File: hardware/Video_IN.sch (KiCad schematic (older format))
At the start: 15 parts, among them U4 DS90CF363AMTD

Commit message: Renaming wires
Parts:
- U4: value DS90CF363AMTD -> DS90CF36B
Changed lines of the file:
@@
 P 7300 3000
 F 0 "U4" H 7300 4770 50  0000 C CNN
-F 1 "DS90CF363AMTD" H 7300 4679 50  0000 C CNN
+F 1 "DS90CF36B" H 7300 4679 50  0000 C CNN
 F 2 "DS90CF364AMTD:SOP50P800X110-48N" H 7300 3000 50  0001 L BNN
 F 3 "41K1941" H 7300 3000 50  0001 L BNN

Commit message: Routing board
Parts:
- R16: renamed from R?; footprint (none) -> Resistor_SMD:R_0805_2012Metric
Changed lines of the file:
@@
 	3550 1850 3650 1850
 $Comp
-L antena:R R?
+L antena:R R16
 U 1 1 5E326151
 P 5750 4600
-F 0 "R?" V 5850 4600 50  0000 C CNN
+F 0 "R16" V 5850 4600 50  0000 C CNN
 F 1 "10K" V 5634 4600 50  0000 C CNN
-F 2 "" V 5680 4600 50  0001 C CNN
+F 2 "Resistor_SMD:R_0805_2012Metric" V 5680 4600 50  0001 C CNN
 F 3 "~" H 5750 4600 50  0001 C CNN
 	1    5750 4600

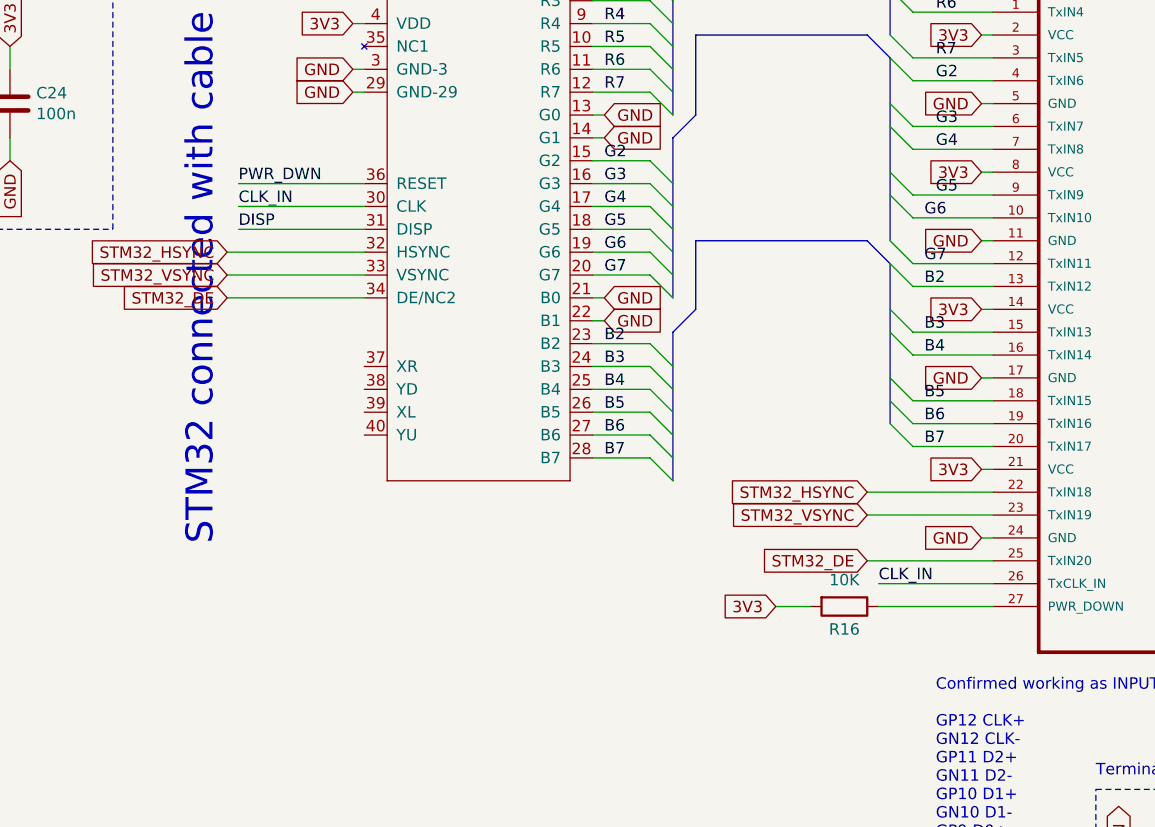
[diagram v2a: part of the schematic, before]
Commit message: Before AGND - GND
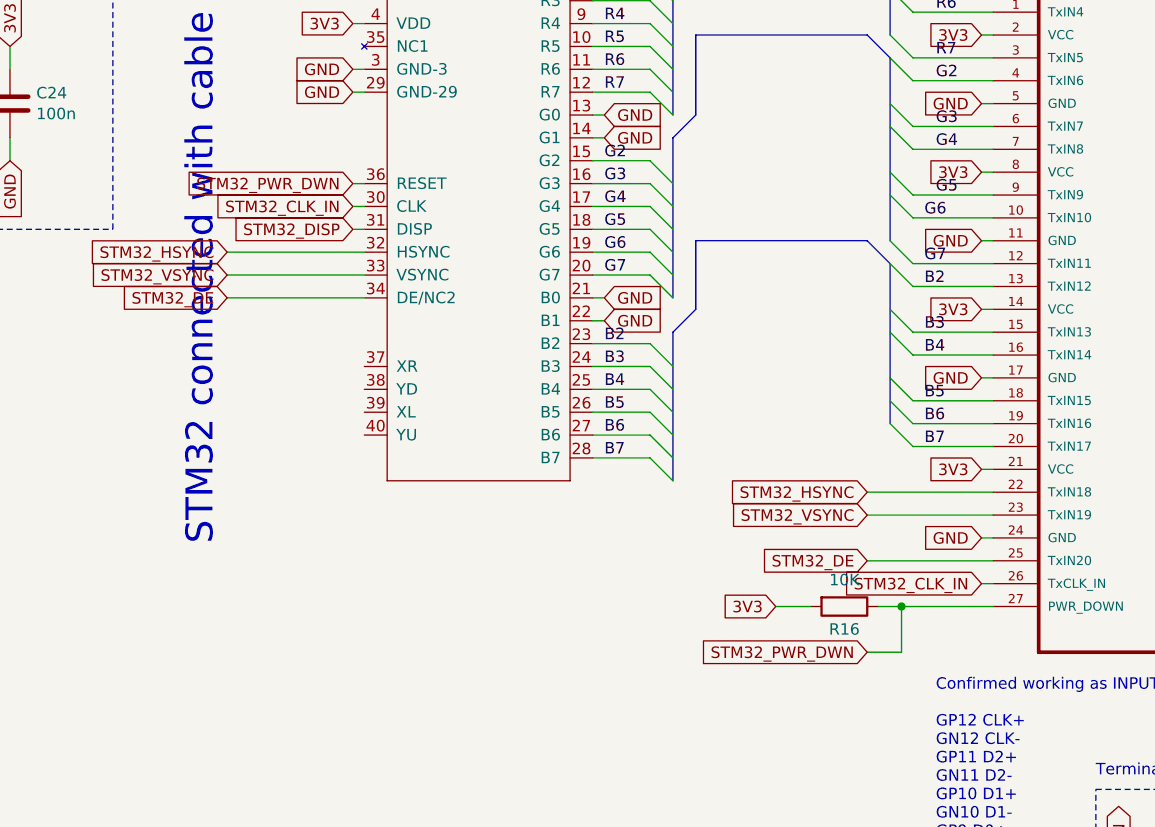
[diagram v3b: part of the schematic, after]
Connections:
- net PWR_DWN is gone; now on net STM32_PWR_DWN: LCD_IN1.36 (RESET)
- net STM32_PWR_DWN: now reaches R16.1, U4.27 (PWR_DOWN)
- net CLK_IN renamed STM32_CLK_IN
- net DISP renamed STM32_DISP
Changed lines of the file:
@@
 	1    0    0    -1
 $EndComp
-Entry Wire Line
-	4900 1850 5000 1950
-Entry Wire Line
-	4900 1950 5000 2050
-Entry Wire Line
-	4900 2050 5000 2150
-Entry Wire Line
-	4900 2150 5000 2250
-Entry Wire Line
-	4900 2250 5000 2350
-Entry Wire Line
-	4900 2350 5000 2450
 Wire Wire Line
 	4650 1850 4900 1850
@@
 Text Label 4700 2350 0    50   ~ 0
 R7
-Entry Wire Line
-	5950 1600 6050 1700
-Entry Wire Line
-	5950 1500 6050 1600
-Entry Wire Line
-	5950 1700 6050 1800
-Entry Wire Line
-	5950 1800 6050 1900
-Entry Wire Line
-	5950 1900 6050 2000
-Entry Wire Line
-	5950 2100 6050 2200
-Wire Wire Line
-	6050 1600 6400 1600
-Wire Wire Line
-	6050 1700 6400 1700
 Wire Wire Line
 	6050 1800 6400 1800
@@
 Wire Wire Line
 	6050 2200 6400 2200
-Text Label 6150 1600 0    50   ~ 0
-R2
-Text Label 6150 1700 0    50   ~ 0
-R3
-Text Label 6150 1800 0    50   ~ 0
-R4
-Text Label 6150 1900 0    50   ~ 0
-R5
-Text Label 6150 2000 0    50   ~ 0
-R6
 Text Label 6150 2200 0    50   ~ 0
 R7
-Entry Wire Line
-	4900 2650 5000 2750
-Entry Wire Line
-	4900 2750 5000 2850
-Entry Wire Line
-	4900 2850 5000 2950
-Entry Wire Line
-	4900 3150 5000 3250
-Entry Wire Line
-	4900 2950 5000 3050
-Entry Wire Line
-	4900 3050 5000 3150
 Wire Wire Line
 	4900 2650 4650 2650
@@
 Wire Wire Line
 	4650 3050 4900 3050
-Entry Wire Line
-	4900 3950 5000 4050
-Entry Wire Line
-	4900 3850 5000 3950
-Entry Wire Line
-	4900 3750 5000 3850
-Entry Wire Line
-	4900 3650 5000 3750
-Entry Wire Line
-	4900 3550 5000 3650
-Entry Wire Line
-	4900 3450 5000 3550
 Wire Wire Line
 	4650 3450 4900 3450
@@
 Text Label 4700 3950 0    50   ~ 0
 B7
-Entry Wire Line
-	5950 2200 6050 2300
-Entry Wire Line
-	5950 2400 6050 2500
-Entry Wire Line
-	5950 2500 6050 2600
-Entry Wire Line
-	5950 2700 6050 2800
-Entry Wire Line
-	5950 2800 6050 2900
-Entry Wire Line
-	5950 3000 6050 3100
 Wire Wire Line
 	6050 2300 6400 2300
@@
 Text Label 6100 3100 0    50   ~ 0
 G7
-Entry Wire Line
-	5950 3100 6050 3200
-Entry Wire Line
-	5950 3300 6050 3400
-Entry Wire Line
-	5950 3400 6050 3500
-Entry Wire Line
-	5950 3700 6050 3800
-Entry Wire Line
-	5950 3600 6050 3700
-Entry Wire Line
-	5950 3800 6050 3900
 Wire Wire Line
 	6050 3200 6400 3200
@@
 Wire Wire Line
 	6350 3300 6400 3300
-Entry Bus Bus
-	5000 2550 5100 2450
-Entry Bus Bus
-	5000 3400 5100 3300
-Entry Bus Bus
-	5000 1750 5100 1650
-Entry Bus Bus
-	5850 1400 5950 1500
-Entry Bus Bus
-	5850 2100 5950 2200
-Entry Bus Bus
-	5850 3000 5950 3100
-Wire Bus Line
-	5100 2450 5100 2100
-Wire Bus Line
-	5100 2100 5850 2100
-Wire Bus Line
-	5100 3300 5100 3000
-Wire Bus Line
-	5100 3000 5850 3000
-Wire Bus Line
-	5100 1650 5100 1400
-Wire Bus Line
-	5100 1400 5850 1400
-Text Label 5900 4500 0    50   ~ 0
-CLK_IN
-Wire Wire Line
-	5900 4500 6400 4500
-Wire Wire Line
-	5900 4600 6400 4600
-Wire Wire Line
-	3650 2850 3100 2850
-Text Label 3100 2850 0    50   ~ 0
-CLK_IN
-Wire Wire Line
-	3650 2750 3100 2750
-Text Label 3100 2750 0    50   ~ 0
-PWR_DWN
-Wire Wire Line
-	3650 2950 3100 2950
-Text Label 3100 2950 0    50   ~ 0
-DISP
 Text Notes 6150 5700 0    50   ~ 0
 Confirmed working as INPUT\n\nGP12 CLK+\nGN12 CLK-\nGP11 D2+\nGN11 D2-\nGP10 D1+\nGN10 D1-\nGP9 D0+\nGN9 D0-
@@
 Wire Wire Line
 	8200 4250 8250 4250
+Text GLabel 3600 2950 0    50   Input ~ 0
+STM32_DISP
+Text GLabel 3600 2850 0    50   Input ~ 0
+STM32_CLK_IN
+Text GLabel 3600 2750 0    50   Input ~ 0
+STM32_PWR_DWN
+Wire Wire Line
+	3600 2750 3650 2750
+Wire Wire Line
+	3600 2850 3650 2850
+Wire Wire Line
+	3600 2950 3650 2950
+Text GLabel 6350 4500 0    50   Input ~ 0
+STM32_CLK_IN
+Text Label 6150 2000 0    50   ~ 0
+R6
+Text Label 6150 1900 0    50   ~ 0
+R5
+Text Label 6150 1800 0    50   ~ 0
+R4
+Text Label 6150 1700 0    50   ~ 0
+R3
+Text Label 6150 1600 0    50   ~ 0
+R2
+Entry Wire Line
+	4900 3950 5000 4050
+Entry Wire Line
+	4900 3850 5000 3950
+Entry Wire Line
+	4900 3750 5000 3850
+Entry Wire Line
+	4900 3650 5000 3750
+Entry Wire Line
+	4900 3550 5000 3650
+Entry Wire Line
+	4900 3450 5000 3550
+Entry Wire Line
+	4900 3150 5000 3250
+Entry Wire Line
+	4900 3050 5000 3150
+Entry Wire Line
+	4900 2950 5000 3050
+Entry Wire Line
+	4900 2850 5000 2950
+Entry Wire Line
+	4900 2750 5000 2850
+Entry Wire Line
+	4900 2650 5000 2750
+Entry Wire Line
+	4900 1850 5000 1950
+Entry Wire Line
+	4900 1950 5000 2050
+Entry Wire Line
+	4900 2250 5000 2350
+Entry Wire Line
+	4900 2050 5000 2150
+Entry Wire Line
+	4900 2150 5000 2250
+Entry Wire Line
+	4900 2350 5000 2450
+Entry Bus Bus
+	5000 2550 5100 2450
+Wire Bus Line
+	5100 2450 5100 2100
+Entry Wire Line
+	5950 3800 6050 3900
+Entry Wire Line
+	5950 3700 6050 3800
+Entry Wire Line
+	5950 3600 6050 3700
+Entry Wire Line
+	5950 3400 6050 3500
+Entry Wire Line
+	5950 3300 6050 3400
+Entry Wire Line
+	5950 3100 6050 3200
+Entry Wire Line
+	5950 3000 6050 3100
+Entry Wire Line
+	5950 2800 6050 2900
+Entry Wire Line
+	5950 2700 6050 2800
+Entry Wire Line
+	5950 2500 6050 2600
+Entry Wire Line
+	5950 2400 6050 2500
+Entry Wire Line
+	5950 2200 6050 2300
+Entry Bus Bus
+	5850 3000 5950 3100
+Entry Bus Bus
+	5000 3400 5100 3300
+Wire Bus Line
+	5100 3300 5100 3000
+Wire Bus Line
+	5100 3000 5850 3000
+Entry Bus Bus
+	5850 2100 5950 2200
+Entry Wire Line
+	5950 2100 6050 2200
+Entry Wire Line
+	5950 1800 6050 1900
+Entry Wire Line
+	5950 1700 6050 1800
+Wire Wire Line
+	6050 1700 6400 1700
+Wire Wire Line
+	6050 1600 6400 1600
+Entry Wire Line
+	5950 1600 6050 1700
+Entry Bus Bus
+	5850 1400 5950 1500
+Entry Wire Line
+	5950 1500 6050 1600
+Entry Wire Line
+	5950 1900 6050 2000
+Wire Bus Line
+	5100 2100 5850 2100
+Entry Bus Bus
+	5000 1750 5100 1650
+Wire Bus Line
+	5100 1650 5100 1400
+Wire Bus Line
+	5100 1400 5850 1400
+Wire Wire Line
+	6350 4500 6400 4500
+Text GLabel 5850 4800 0    50   Input ~ 0
+STM32_PWR_DWN
+Wire Wire Line
+	5850 4800 6000 4800
+Wire Wire Line
+	6000 4800 6000 4600
+Wire Wire Line
+	5900 4600 6000 4600
 Wire Bus Line
 	5950 1500 5950 2100
@@
 Wire Bus Line
 	5000 3400 5000 4050
+Wire Wire Line
+	6000 4600 6400 4600
+Connection ~ 6000 4600
 $EndSCHEMATC
